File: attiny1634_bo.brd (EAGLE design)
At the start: 49.5 x 22.2 mm, 11 parts, among them J1 AVR_SPI_PRG_6NS, Y1 12MHz

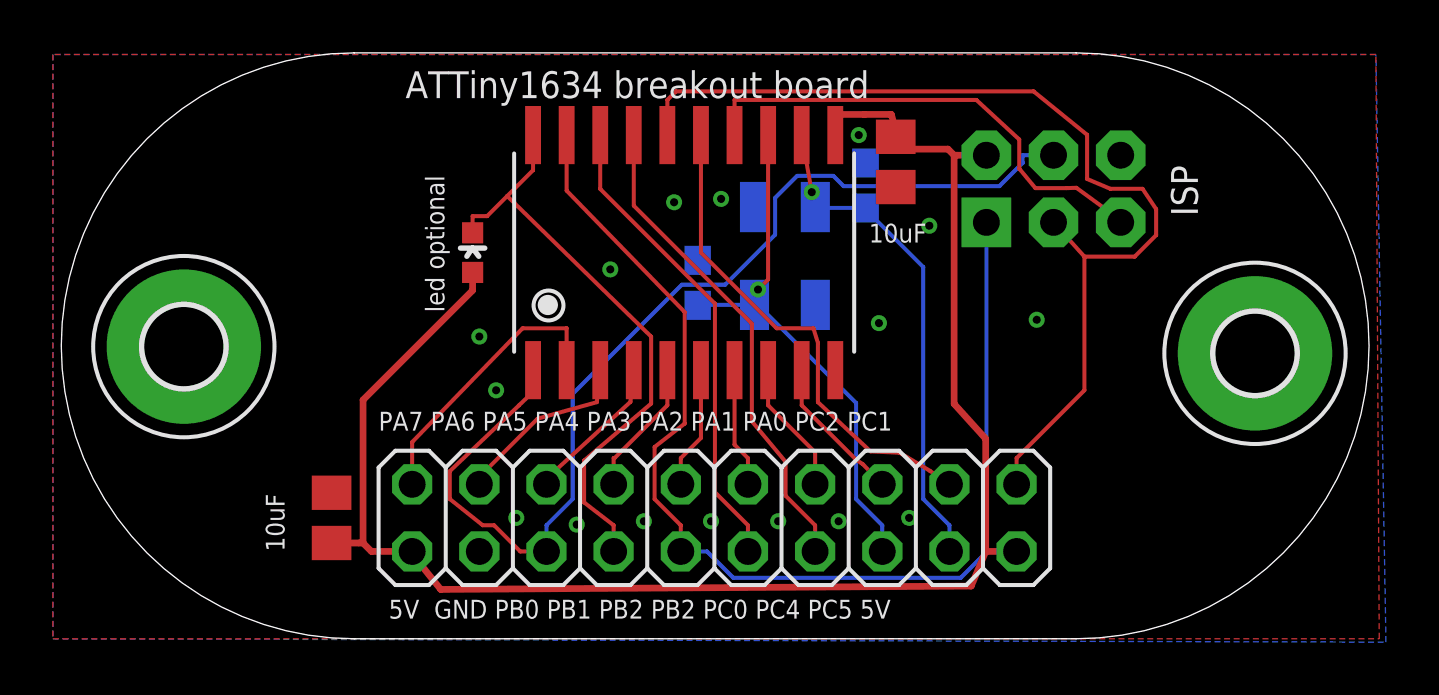
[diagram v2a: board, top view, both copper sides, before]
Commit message: shite, the MOSI is was marked to wrong pin...
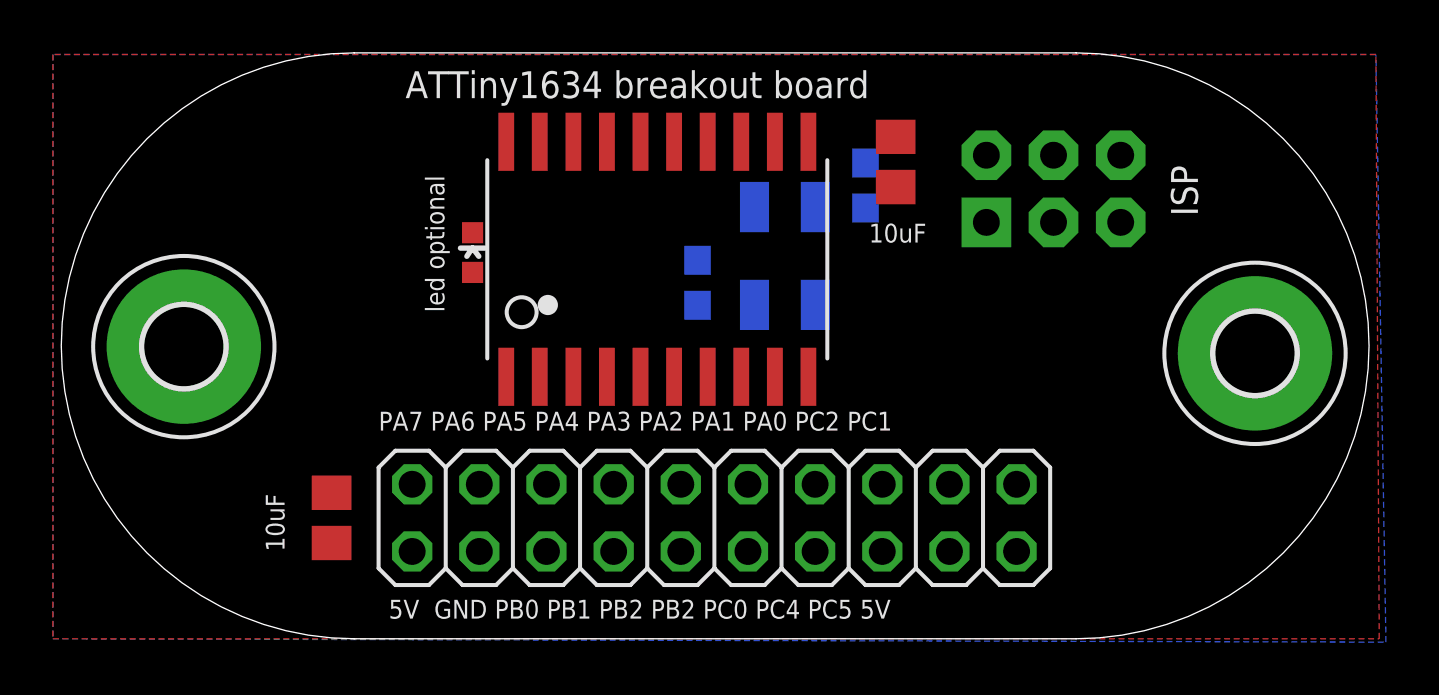
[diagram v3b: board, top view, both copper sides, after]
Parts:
- moved U$1 1.05 mm to (19.1, 14.4)
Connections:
- removed net PB0/MOSI/TX0/ADC5: J1.4, JP1.16, U$1.1
- new net PB0/TXD0: U$1.1
- new net PB1/MOSI/ADC6: J1.4, JP1.16, U$1.20
- net PA0: no longer U$1.9
- net PA1: no longer U$1.8
- net PA2: no longer U$1.7
- net PA3: no longer U$1.6
- net PA4: no longer U$1.5
- net PA5: no longer U$1.4
- net PA6: no longer U$1.3
- net PA7: no longer U$1.2
- net PB1/ADC6/RX1: no longer LED1.C, U$1.20
- net PC0/ADC9/OC0A: now also LED1.C
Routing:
- net +5V: track 63.2 -> 0.00 mm
- net PB2/ADC7/TX1: track 43.4 -> 0.00 mm
- net PB0/MOSI/TX0/ADC5: track 40.2 -> 0.00 mm
- net PC1/SCL/ADC10: track 38.1 -> 0.00 mm
- net PB1/ADC6/RX1: track 22.4 -> 0.00 mm
- net PC4/XTAL2: track 20.2 -> 0.00 mm, vias 1 -> 0
- net PC5/XTAL1: track 19.0 -> 0.00 mm, vias 1 -> 0
- net PC2/ADC11: track 18.8 -> 0.00 mm
- net PC0/ADC9/OC0A: track 18.5 -> 0.00 mm
- net PC3/-RESET: track 18.4 -> 0.00 mm
- net PB3/ADC8/OC1A: track 18.1 -> 0.00 mm
- net PA7: track 10.8 -> 0.00 mm
- net PA6: track 6.89 -> 0.00 mm
- net PA5: track 5.71 -> 0.00 mm
- net PA0: track 5.60 -> 0.00 mm
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
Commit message: add a resistor for the led and move the mcu group right, in preparation for adding a uart header
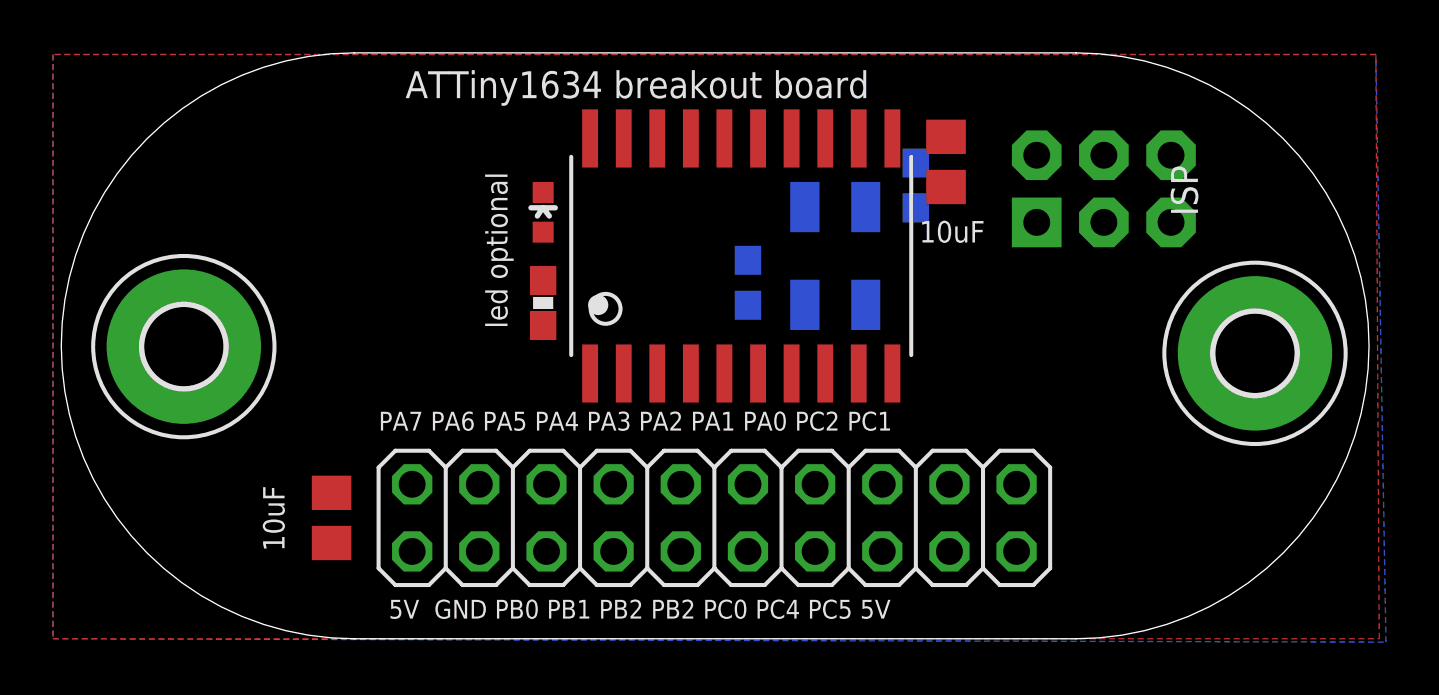
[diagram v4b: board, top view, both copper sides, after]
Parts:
- added RLED1: 330, SparkFun-Passives:0603-RES
- moved U$1 3.18 mm to (22.2, 14.5)
- moved LED1 3.07 mm to (18.5, 16.1)
- moved CX0 1.91 mm to (26.3, 13.5)
- moved CX1 1.91 mm to (32.6, 17.1)
- moved J1 1.91 mm to (39.8, 17.0)
- moved Y1 1.91 mm to (29.6, 14.5)
- moved C1 1.90 mm to (33.8, 18.0)
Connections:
- new net N$1: LED1.A, RLED1.1
- net +5V: now also RLED1.2; no longer LED1.A
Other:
- board text added: "XTAL optional (12MHz)"
- board text removed: "XTAL optional"

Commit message: space for cable
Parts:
- added FTDI: (no value), pinhead:1X06
- moved C2 1.49 mm to (11.0, 3.17), turned to 180 degrees
- moved JP1 1.40 mm to (26.4, 4.45)
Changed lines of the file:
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@@
 <text x="13.335" y="20.447" size="1.016" layer="25" font="vector" ratio="10">ATTiny1634 breakout board</text>
 <text x="42.291" y="17.907" size="1.016" layer="25" font="vector" ratio="10" rot="R270">ISP</text>
-<text x="37.338" y="7.874" size="0.7112" layer="26" font="vector" ratio="15" rot="MR0">PC1 PC2 PA0 PA1 PA2 PA3 PA4 PA5 PA6 PA7</text>
-<text x="37.084" y="0.762" size="0.7112" layer="26" font="vector" ratio="15" rot="MR0">5V PC5 PC3 PC0 PB3 PB2 PB1 PB0 GND 5V</text>
-<text x="12.319" y="7.874" size="0.7112" layer="25" font="vector" ratio="15">PA7 PA6 PA5 PA4 PA3 PA2 PA1 PA0 PC2 PC1</text>
-<text x="12.7" y="0.762" size="0.7112" layer="25" font="vector" ratio="15">5V  GND PB0 PB1 PB2 PB2 PC0 PC4 PC5 5V</text>
-<text x="24.765" y="14.097" size="0.8128" layer="26" font="vector" ratio="10" rot="MR0">XTAL optional (12MHz)</text>
+<text x="38.735" y="7.747" size="0.7112" layer="26" font="vector" ratio="15" rot="MR0">PC1 PC2 PA0 PA1 PA2 PA3 PA4 PA5 PA6 PA7</text>
+<text x="38.481" y="0.635" size="0.7112" layer="26" font="vector" ratio="15" rot="MR0">5V PC5 PC3 PC0 PB3 PB2 PB1 PB0 GND 5V</text>
+<text x="13.716" y="7.747" size="0.7112" layer="25" font="vector" ratio="15">PA7 PA6 PA5 PA4 PA3 PA2 PA1 PA0 PC2 PC1</text>
+<text x="14.097" y="0.635" size="0.7112" layer="25" font="vector" ratio="15">5V  GND PB0 PB1 PB2 PB2 PC0 PC4 PC5 5V</text>
+<text x="27.432" y="16.51" size="0.8128" layer="26" font="vector" ratio="10" rot="MR0">XTAL optional (12MHz)</text>
 <text x="16.383" y="17.653" size="0.8128" layer="25" font="vector" ratio="10" rot="R270">led optional</text>
-<text x="8.763" y="3.302" size="0.8128" layer="25" font="vector" ratio="10" rot="R90">10uF</text>
+<text x="8.509" y="2.286" size="0.8128" layer="25" font="vector" ratio="10" rot="R90">10uF</text>
 <text x="32.766" y="14.986" size="0.8128" layer="25" font="vector" ratio="10">10uF</text>
-<text x="24.892" y="12.319" size="0.8128" layer="26" ratio="10" rot="MR0">12pF caps for xtal</text>
+<text x="25.781" y="15.367" size="0.8128" layer="26" ratio="10" rot="MR0">12pF caps for xtal</text>
 <circle x="20.6248" y="12.6238" radius="0.179603125" width="0.4064" layer="25"/>
 </plain>
@@
 <attribute name="VALUE" x="19.6215" y="15.113" size="0.4064" layer="27" rot="R90"/>
 </element>
-<element name="C2" library="rcl" package="C0805" value="" x="10.541" y="4.572" smashed="yes" rot="R90">
-<attribute name="VALUE" x="13.081" y="3.302" size="1.27" layer="27" rot="R90"/>
+<element name="C2" library="rcl" package="C0805" value="" x="11.049" y="3.175" smashed="yes" rot="R180">
+<attribute name="VALUE" x="12.319" y="5.715" size="1.27" layer="27" rot="R180"/>
 </element>
 <element name="CX0" library="rcl" package="C0603" value="22pF" x="26.289" y="13.462" smashed="yes" rot="MR270"/>
@@
 <element name="H1" library="holes" package="3,0-PAD" value="MOUNT-PAD-ROUND3.0" x="4.953" y="11.049"/>
 <element name="H2" library="holes" package="3,0-PAD" value="MOUNT-PAD-ROUND3.0" x="45.466" y="10.795"/>
-<element name="JP1" library="pinhead" package="2X10" value="" x="25.019" y="4.572" smashed="yes" rot="R180">
-<attribute name="VALUE" x="37.719" y="9.017" size="1.27" layer="27" rot="R180"/>
+<element name="JP1" library="pinhead" package="2X10" value="" x="26.416" y="4.445" smashed="yes" rot="R180">
+<attribute name="VALUE" x="39.116" y="8.89" size="1.27" layer="27" rot="R180"/>
 </element>
 <element name="U$1" library="attiny1634" package="SOIC20" value="ATTINY1634" x="22.225" y="14.478" smashed="yes"/>
 <element name="RLED1" library="SparkFun-Passives" package="0603-RES" value="330" x="18.542" y="12.7" smashed="yes" rot="R270"/>
+<element name="FTDI" library="pinhead" package="1X06" value="" x="11.303" y="12.319" smashed="yes" rot="R90">
+<attribute name="NAME" x="14.8082" y="11.0998" size="1.27" layer="25" ratio="10" rot="R90"/>
+<attribute name="VALUE" x="14.478" y="4.699" size="1.27" layer="27" rot="R90"/>
+</element>
 </elements>
 <signals>
@@
 <wire x1="31.75" y1="18.923" x2="33.782" y2="18.984" width="0" layer="19" extent="1-1"/>
 <wire x1="18.542" y1="11.85" x2="31.75" y2="18.923" width="0" layer="19" extent="1-1"/>
-<wire x1="13.589" y1="3.302" x2="18.542" y2="11.85" width="0" layer="19" extent="1-1"/>
-<wire x1="10.541" y1="3.622" x2="13.589" y2="3.302" width="0" layer="19" extent="1-1"/>
-<wire x1="36.449" y1="3.302" x2="37.211" y2="18.288" width="0" layer="19" extent="1-1"/>
+<wire x1="14.986" y1="3.175" x2="18.542" y2="11.85" width="0" layer="19" extent="1-1"/>
+<wire x1="11.999" y1="3.175" x2="14.986" y2="3.175" width="0" layer="19" extent="1-1"/>
+<wire x1="37.846" y1="3.175" x2="37.211" y2="18.288" width="0" layer="19" extent="1-1"/>
 </signal>
 <signal name="PB1/ADC6/RX1">
@@
 <contactref element="JP1" pad="1"/>
 <contactref element="U$1" pad="16"/>
-<wire x1="36.449" y1="5.842" x2="39.751" y2="15.748" width="0" layer="19" extent="1-1"/>
+<wire x1="37.846" y1="5.715" x2="39.751" y2="15.748" width="0" layer="19" extent="1-1"/>
 <wire x1="25.4" y1="18.923" x2="39.751" y2="15.748" width="0" layer="19" extent="1-1"/>
 </signal>
@@
 <contactref element="U$1" pad="19"/>
 <wire x1="21.59" y1="18.923" x2="37.211" y2="15.748" width="0" layer="19" extent="1-1"/>
-<wire x1="23.749" y1="3.302" x2="21.59" y2="18.923" width="0" layer="19" extent="1-1"/>
+<wire x1="25.146" y1="3.175" x2="21.59" y2="18.923" width="0" layer="19" extent="1-1"/>
 </signal>
 <signal name="PC3/-RESET">
@@
 <wire x1="30.741" y1="16.328" x2="30.48" y2="18.923" width="0" layer="19" extent="1-16"/>
 <wire x1="32.639" y1="16.295" x2="30.741" y2="16.328" width="0" layer="19" extent="16-16"/>
-<wire x1="33.909" y1="3.302" x2="32.639" y2="16.295" width="0" layer="19" extent="16-16"/>
+<wire x1="35.306" y1="3.175" x2="32.639" y2="16.295" width="0" layer="19" extent="16-16"/>
 </signal>
 <signal name="PC4/XTAL2">
@@
 <wire x1="28.441" y1="12.628" x2="29.21" y2="18.923" width="0" layer="19" extent="1-16"/>
 <wire x1="26.289" y1="12.612" x2="28.441" y2="12.628" width="0" layer="19" extent="16-16"/>
-<wire x1="31.369" y1="3.302" x2="28.441" y2="12.628" width="0" layer="19" extent="16-16"/>
+<wire x1="32.766" y1="3.175" x2="28.441" y2="12.628" width="0" layer="19" extent="16-16"/>
 </signal>
 <signal name="PA0">
@@
 <contactref element="JP1" pad="10"/>
 <contactref element="U$1" pad="18"/>
-<wire x1="26.289" y1="3.302" x2="22.86" y2="18.923" width="0" layer="19" extent="1-1"/>
+<wire x1="27.686" y1="3.175" x2="22.86" y2="18.923" width="0" layer="19" extent="1-1"/>
 </signal>
 <signal name="PC0/ADC9/OC0A">
@@
 <contactref element="LED1" pad="C"/>
 <wire x1="18.542" y1="16.879" x2="24.13" y2="18.923" width="0" layer="19" extent="1-1"/>
-<wire x1="28.829" y1="3.302" x2="24.13" y2="18.923" width="0" layer="19" extent="1-1"/>
+<wire x1="30.226" y1="3.175" x2="24.13" y2="18.923" width="0" layer="19" extent="1-1"/>
 </signal>
 <signal name="PC2/ADC11">
 <contactref element="JP1" pad="3"/>
 <contactref element="U$1" pad="15"/>
-<wire x1="33.909" y1="5.842" x2="26.67" y2="18.923" width="0" layer="19" extent="1-1"/>
+<wire x1="35.306" y1="5.715" x2="26.67" y2="18.923" width="0" layer="19" extent="1-1"/>
 </signal>
 <signal name="PB0/TXD0">
@@
 <contactref element="JP1" pad="16"/>
 <wire x1="20.32" y1="18.923" x2="39.751" y2="18.288" width="0" layer="19" extent="1-1"/>
-<wire x1="18.669" y1="3.302" x2="20.32" y2="18.923" width="0" layer="19" extent="1-1"/>
+<wire x1="20.066" y1="3.175" x2="20.32" y2="18.923" width="0" layer="19" extent="1-1"/>
 </signal>
 <signal name="N$1">
